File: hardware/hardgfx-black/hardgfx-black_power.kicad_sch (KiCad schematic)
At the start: 61 parts, among them J1 Input Voltage, J10 Conn_01x02, J11 Conn_01x02, J2 Conn_01x02, J3 Conn_01x02, J4 Conn_01x02, J5 Conn_01x02, J6 Conn_01x02, J7 Conn_01x02, J8 Conn_01x02, J9 Conn_01x02, U1 STM32H745BITx, U2 MIC4575-5.0WU, U3 ST1L05APU33R, U4 LD1117S18TR

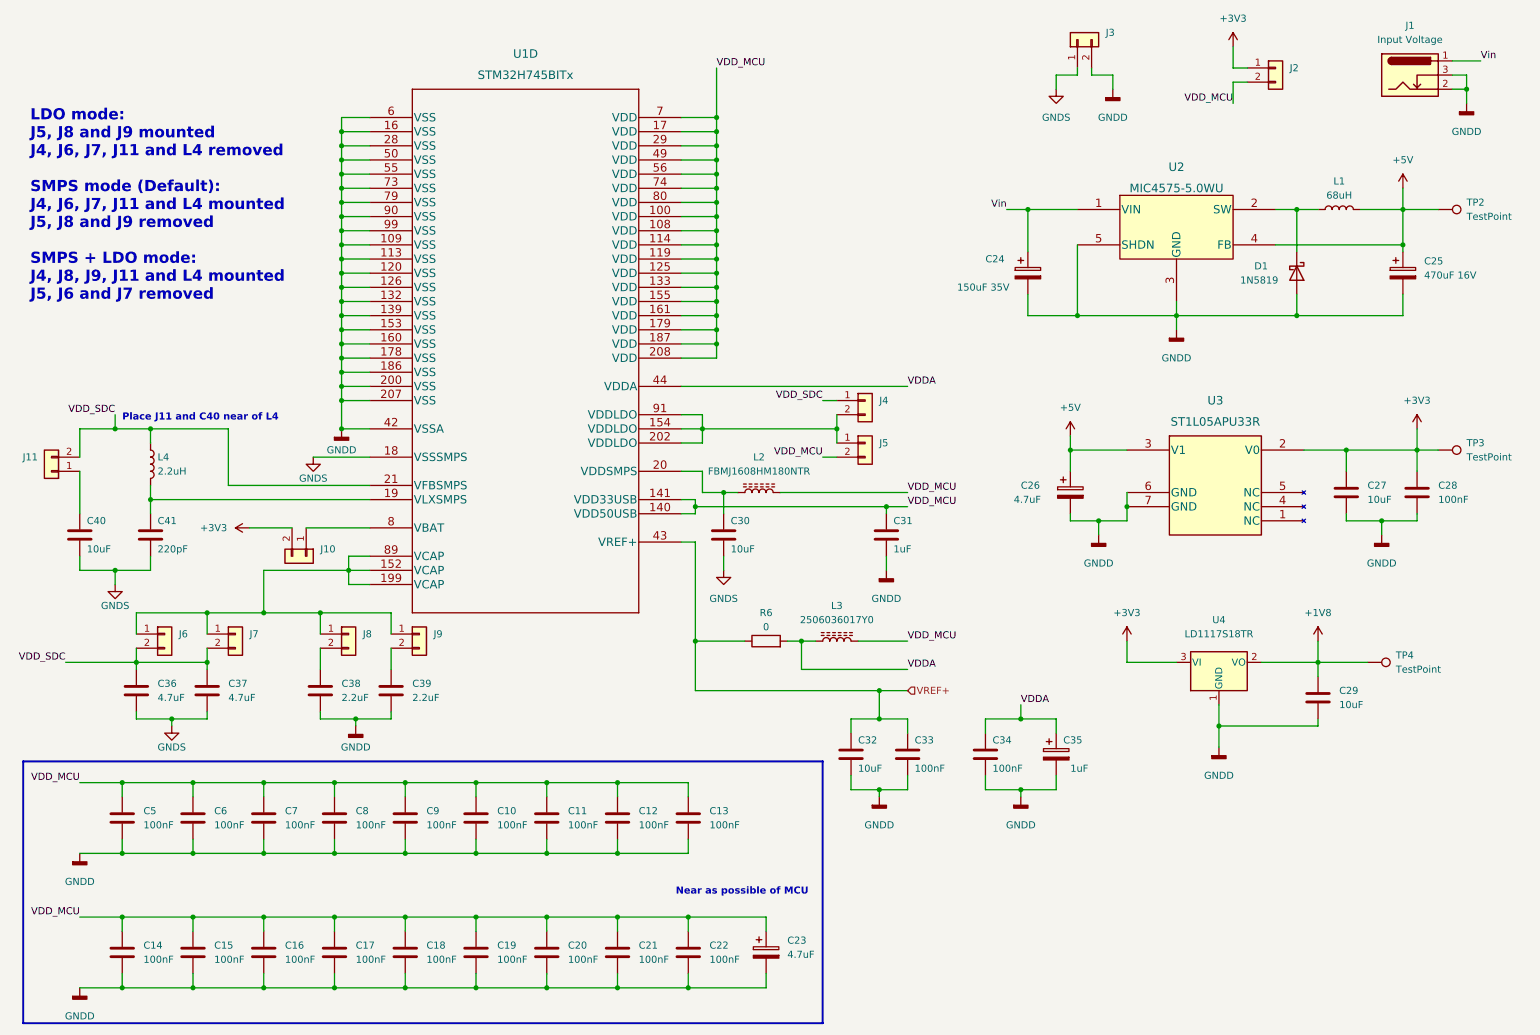
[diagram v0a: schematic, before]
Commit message: Finish first schematic version.
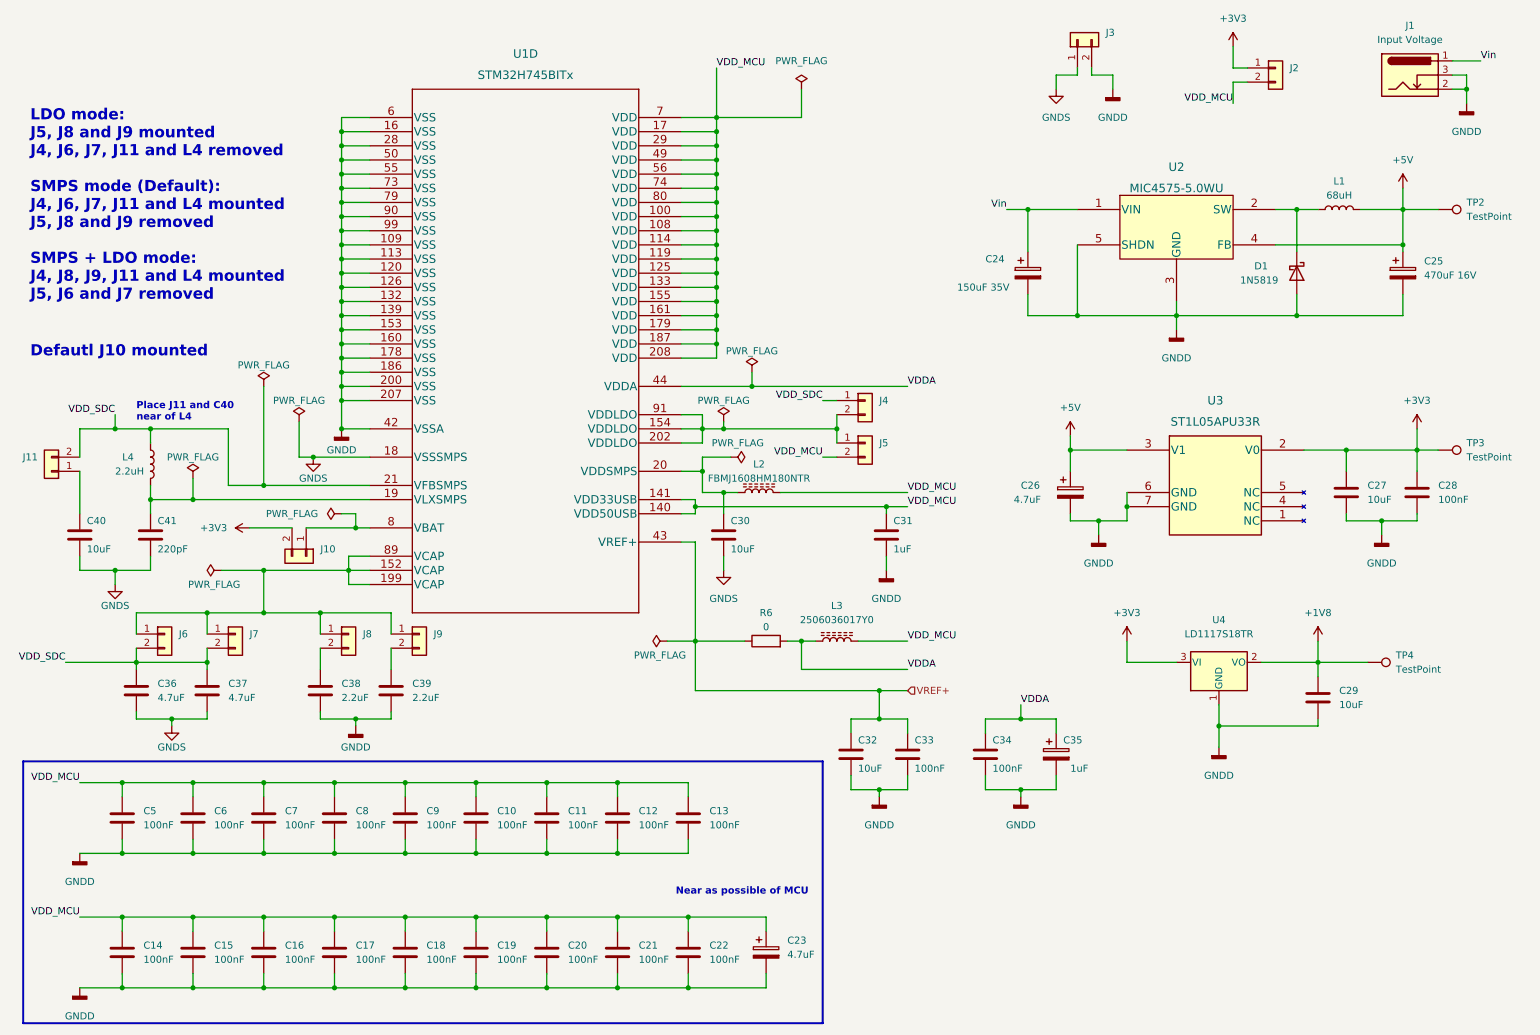
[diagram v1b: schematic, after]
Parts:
- J10, J11, J2, J3, J4, J5, J6, J7, J8, J9: MANUFACTURER Molex -> Samtec Inc.; digikey# 0423752486-ND -> SAM1029-02-ND; manf# 0423752486 -> TSW-102-07-G-S; mouser# 538-42375-2486 -> 200-TSW10207GS
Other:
- note added: "Defautl J10 mounted"
